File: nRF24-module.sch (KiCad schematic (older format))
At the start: 43 parts, among them SW1 SW_PUSH, U1 STM32F302C8T, U2 SN65HVD256, U3 NUF2042XV6, U4 MCP1700, U5 SiP32431, X1 16MHz 10ppm

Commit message: nRF pin assignment.
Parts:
- removed C10, C14, C16: 100nF, _std:_0603, symbol C
- removed C15: 1uF, _std:_0603, symbol C
- removed C6: 10nF, _std:_0603, symbol C
- removed CONN1: UART, _connectors:Molex-PicoBlade-4, symbol UART
- removed D3: V_BUS_PWR, _std:_0603, symbol LED
- removed R10, R11: 100, _std:_0603, symbol R
- removed R3, R4, R9: 10k, _std:_0603, symbol R
- removed R7: R, _std:_0603, symbol R
- removed U5: SiP32431, Housings_SOT-23_SOT-143_TSOT-6:SC-70-6, symbol SiP32431
- added D3, D4: BAT60J, _std:_SOD-323, symbol D
- added P1: CONN_02X04, Pin_Headers:Pin_Header_Straight_2x04, symbol CONN_02X04
- CONN2: renamed from CONN3; footprint _connectors:_Micro-USB-AB-receptacle-SMT-th -> _connectors:_Micro-USB-AB-receptacle-SMT
- D1: value STATUS -> nRF
- D2: value CAN1 -> CAN
- renumbered C13 to C10, C12 to C11, C5 to C4, C4 to C5, C7 to C6, C8 to C7, C9 to C8, C11 to C9, CONN2 to CONN1, CONN4 to CONN3, CONN5 to CONN4, R5 to R3, R6 to R4, R8 to R5
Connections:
- net labels added: +5V, CAN_ACTIVITY_LED, RF_ACTIVITY_LED, nRF_CE, nRF_CSN, nRF_IRQ, nRF_MISO, nRF_MOSI, nRF_SCK
- net labels removed: CAN1_PWR_LED, CAN1_STATUS_LED, CAN_SILENT, STATUS_LED, UART1_RX, UART1_TX, V_BUS_ENABLE, V_BUS_SENSE
- wire segments 109 -> 87
- no-connect marks 21 -> 23
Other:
- note added: "04.11.2015"
- note added: "<-JTCK"
- note added: "<-JTDI"
- note added: "<-JTDO"
- note added: "<-JTMS"
- note added: "<-JTRST"
- note added: "nRF24 module radio module"
- note removed: "(5V tolerant)"
- note removed: "25.10.2015"
- note removed: "CAN to USB adapter dongle"
- note removed: "Fc = 318 Hz\n(10k+10k)/(10k*10k*100nF*2*pi)"
- moved on the sheet: C10, C11, C9, CONN1, CONN2, CONN3, CONN4, F1, R5, U2, U3

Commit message: No dfu pushbutton
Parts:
- removed R2: 10k, _std:_0603, symbol R
- removed SW1: SW_PUSH, _div:PushButtonSMD-5x3mm, symbol SW_PUSH
- added C12: 22uF, _std:_0603, symbol C
- CONN1: footprint _connectors:_Solder_Pad1.27_5 -> _connectors:_Pin2mm_5z
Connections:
- net labels removed: BOOT0
- wire segments 87 -> 83
- no-connect marks 23 -> 24
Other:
- note removed: "enter dfu bootloader\nby pressing the button\nwhen plugging in the dongle"
- moved on the sheet: CONN1, D1, D2, D3, D4, P1, R3, R4

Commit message: Change voltage regulator
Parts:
- removed U4: MCP1700, _std:SOT-23, symbol MCP1700
- added U4: MCP1703, symbol MCP1703
- renumbered C9 to C10, C10 to C11, C11 to C12, C12 to C9, R3 to R2, R4 to R3, R5 to R4
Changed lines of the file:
@@
 $EndComp
 $Comp
-L R R4
+L R R3
 U 1 1 55622F4C
 P 5050 1650
-F 0 "R4" V 5130 1650 50  0000 C CNN
+F 0 "R3" V 5130 1650 50  0000 C CNN
 F 1 "R" V 5050 1650 50  0000 C CNN
 F 2 "_std:_0603" V 4980 1650 30  0001 C CNN
@@
 $EndComp
 $Comp
-L R R3
+L R R2
 U 1 1 5562427A
 P 5050 1350
-F 0 "R3" V 5130 1350 50  0000 C CNN
+F 0 "R2" V 5130 1350 50  0000 C CNN
 F 1 "R" V 5050 1350 50  0000 C CNN
 F 2 "_std:_0603" V 4980 1350 30  0001 C CNN
@@
 $EndComp
 $Comp
-L MCP1700 U4
-U 1 1 55D2FCCD
-P 9400 1600
-F 0 "U4" H 9650 1800 60  0000 C CNN
-F 1 "MCP1700" H 9350 1800 60  0000 C CNN
-F 2 "_std:SOT-23" H 9300 2050 60  0001 C CNN
-F 3 "" H 9300 2050 60  0000 C CNN
-	1    9400 1600
-	1    0    0    -1
-$EndComp
-$Comp
-L C C9
+L C C10
 U 1 1 55D2FDCA
 P 8850 1750
-F 0 "C9" H 8875 1850 50  0000 L CNN
+F 0 "C10" H 8875 1850 50  0000 L CNN
 F 1 "1uF" H 8875 1650 50  0000 L CNN
 F 2 "_std:_0603" H 8888 1600 30  0001 C CNN
@@
 $EndComp
 $Comp
-L C C11
+L C C12
 U 1 1 55D2FE2A
 P 9950 1750
-F 0 "C11" H 9975 1850 50  0000 L CNN
+F 0 "C12" H 9975 1850 50  0000 L CNN
 F 1 "1uF" H 9975 1650 50  0000 L CNN
 F 2 "_std:_0603" H 9988 1600 30  0001 C CNN
@@
 Author: Michael Spieler
 $Comp
-L C C10
+L C C11
 U 1 1 560BF88C
 P 9750 2950
-F 0 "C10" H 9800 2850 50  0000 L CNN
+F 0 "C11" H 9800 2850 50  0000 L CNN
 F 1 "100nF" V 9600 2850 50  0000 L CNN
 F 2 "_std:_0603" H 9788 2800 30  0001 C CNN
@@
 $EndComp
 $Comp
-L R R5
+L R R4
 U 1 1 560C3883
 P 8000 3000
-F 0 "R5" V 8080 3000 50  0000 C CNN
+F 0 "R4" V 8080 3000 50  0000 C CNN
 F 1 "1.5k" V 8000 3000 50  0000 C CNN
 F 2 "_std:_0603" V 7930 3000 30  0001 C CNN
@@
 NoConn ~ 3600 4900
 NoConn ~ 3600 3500
-$Comp
-L CVRA_logo #G1
-U 1 1 562D3733
-P 10100 6850
-F 0 "#G1" H 10100 6682 60  0001 C CNN
-F 1 "CVRA_logo" H 10100 7018 60  0001 C CNN
-F 2 "" H 10100 6850 60  0000 C CNN
-F 3 "" H 10100 6850 60  0000 C CNN
-	1    10100 6850
-	1    0    0    -1
-$EndComp
 $Comp
 L STM32F302C8T U1
@@
 Wire Wire Line
 	9950 1950 9950 1900
-Connection ~ 9400 1950
 Wire Wire Line
 	9850 5650 9950 5650
@@
 Connection ~ 7750 4650
 $Comp
-L C C12
+L C C9
 U 1 1 563B4E3B
 P 8600 1750
-F 0 "C12" H 8625 1850 50  0000 L CNN
+F 0 "C9" H 8625 1850 50  0000 L CNN
 F 1 "22uF" H 8625 1650 50  0000 L CNN
 F 2 "_std:_0603" H 8638 1600 30  0001 C CNN
@@
 $EndComp
 NoConn ~ 3600 1400
+$Comp
+L MCP1703 U4
+U 1 1 563B6919
+P 9400 1600
+F 0 "U4" H 9650 1800 60  0000 C CNN
+F 1 "MCP1703" H 9350 1800 60  0000 C CNN
+F 2 "" H 9300 2050 60  0000 C CNN
+F 3 "" H 9300 2050 60  0000 C CNN
+	1    9400 1600
+	1    0    0    -1
+$EndComp
+Connection ~ 9400 1950
 $EndSCHEMATC

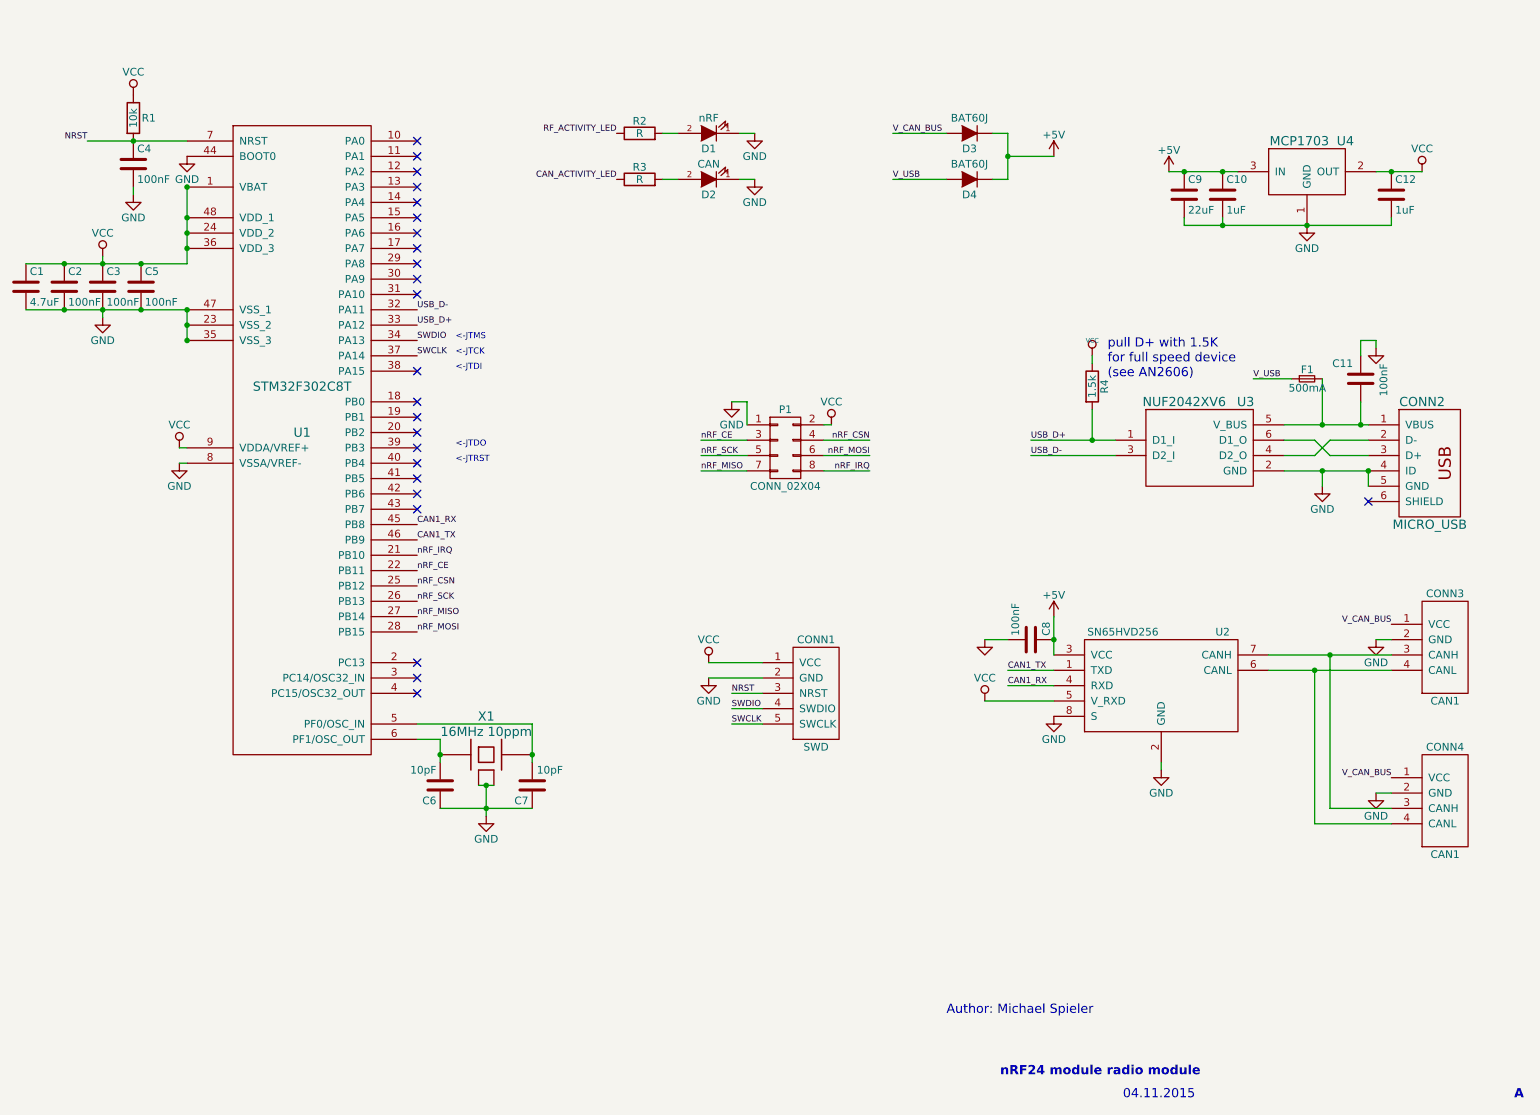
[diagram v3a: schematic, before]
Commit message: Simplify schematic
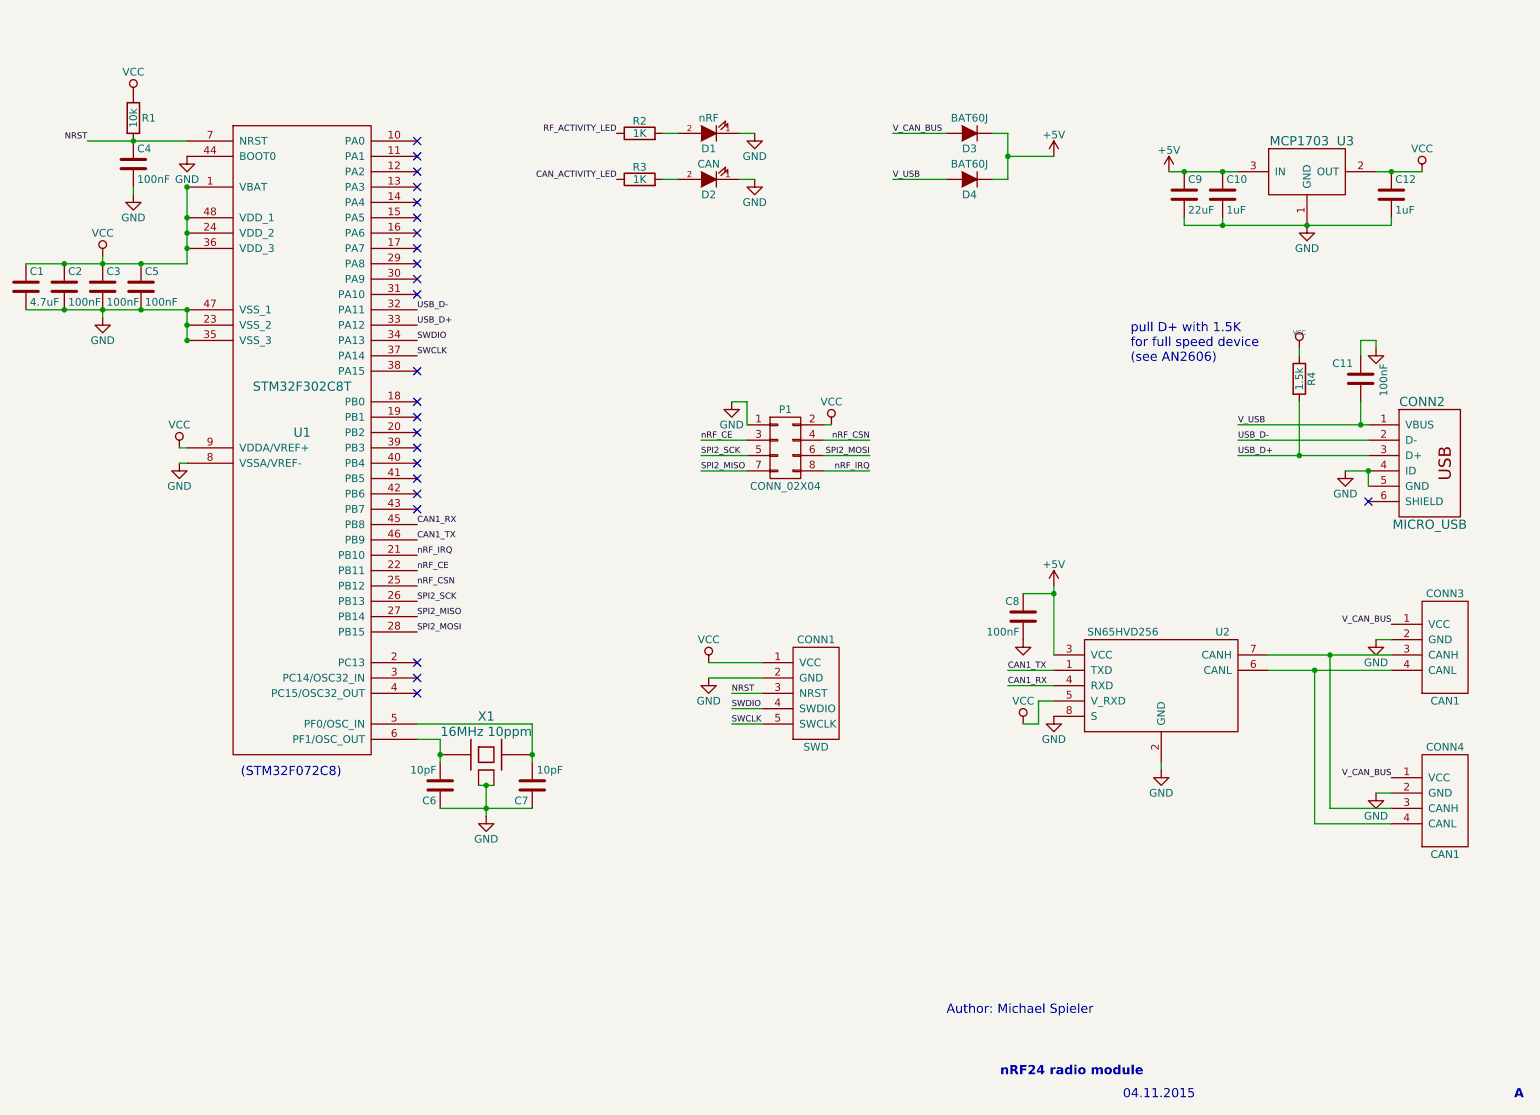
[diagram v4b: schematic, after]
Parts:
- removed F1: 500mA, Resistors_SMD:R_0805, symbol F_Small
- removed U3: NUF2042XV6, _std:SOT-563_6-lead, symbol NUF2042XV6
- R2, R3: value R -> 1K
- renumbered U4 to U3
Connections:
- net USB_D+: now also CONN2.3 (D+)
- net USB_D-: now also CONN2.2 (D-)
- net V_USB: now also C11.1, CONN2.1 (VBUS)
- net nRF_MISO renamed SPI2_MISO
- net nRF_MOSI renamed SPI2_MOSI
- net nRF_SCK renamed SPI2_SCK
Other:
- note added: "(STM32F072C8)"
- note added: "nRF24 radio module"
- note removed: "<-JTCK"
- note removed: "<-JTDI"
- note removed: "<-JTDO"
- note removed: "<-JTMS"
- note removed: "<-JTRST"
- note removed: "nRF24 module radio module"
- moved on the sheet: C8, R4
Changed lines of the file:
@@
 Text Label 3600 2600 0    40   ~ 0
 USB_D+
-Text Label 7600 3450 0    40   ~ 0
+Text Label 8950 3350 0    40   ~ 0
 USB_D-
-Text Label 7600 3350 0    40   ~ 0
+Text Label 8950 3450 0    40   ~ 0
 USB_D+
-Text Label 9050 2950 0    40   ~ 0
+Text Label 8950 3250 0    40   ~ 0
 V_USB
 $Comp
 L GND #PWR08
 U 1 1 55621D6C
-P 9500 3650
-F 0 "#PWR08" H 9500 3400 50  0001 C CNN
-F 1 "GND" H 9500 3500 50  0000 C CNN
-F 2 "" H 9500 3650 60  0000 C CNN
-F 3 "" H 9500 3650 60  0000 C CNN
-	1    9500 3650
+P 9650 3550
+F 0 "#PWR08" H 9650 3300 50  0001 C CNN
+F 1 "GND" H 9650 3400 50  0000 C CNN
+F 2 "" H 9650 3550 60  0000 C CNN
+F 3 "" H 9650 3550 60  0000 C CNN
+	1    9650 3550
 	1    0    0    -1
 $EndComp
@@
 P 5050 1650
 F 0 "R3" V 5130 1650 50  0000 C CNN
-F 1 "R" V 5050 1650 50  0000 C CNN
+F 1 "1K" V 5050 1650 50  0000 C CNN
 F 2 "_std:_0603" V 4980 1650 30  0001 C CNN
 F 3 "" H 5050 1650 30  0000 C CNN
@@
 P 5050 1350
 F 0 "R2" V 5130 1350 50  0000 C CNN
-F 1 "R" V 5050 1350 50  0000 C CNN
+F 1 "1K" V 5050 1350 50  0000 C CNN
 F 2 "_std:_0603" V 4980 1350 30  0001 C CNN
 F 3 "" H 5050 1350 30  0000 C CNN
@@
 L VCC #PWR011
 U 1 1 5592BB1F
-P 7300 5050
-F 0 "#PWR011" H 7300 4900 50  0001 C CNN
-F 1 "VCC" H 7300 5200 50  0000 C CNN
-F 2 "" H 7300 5050 60  0000 C CNN
-F 3 "" H 7300 5050 60  0000 C CNN
-	1    7300 5050
+P 7550 5200
+F 0 "#PWR011" H 7550 5050 50  0001 C CNN
+F 1 "VCC" H 7550 5350 50  0000 C CNN
+F 2 "" H 7550 5200 60  0000 C CNN
+F 3 "" H 7550 5200 60  0000 C CNN
+	1    7550 5200
 	1    0    0    -1
 $EndComp
@@
 Text Label 6700 1650 0    40   ~ 0
 V_USB
-$Comp
-L F_Small F1
-U 1 1 55D30CFC
-P 9400 2950
-F 0 "F1" H 9360 3010 50  0000 L CNN
-F 1 "500mA" H 9280 2890 50  0000 L CNN
-F 2 "Resistors_SMD:R_0805" H 9400 2950 60  0001 C CNN
-F 3 "" H 9400 2950 60  0000 C CNN
-	1    9400 2950
-	1    0    0    -1
-$EndComp
 Text Label 6700 1350 0    40   ~ 0
 V_CAN_BUS
@@
 $EndComp
 Text Notes 7400 7500 0    60   ~ 12
-nRF24 module radio module
+nRF24 radio module
 Text Notes 10750 7650 0    60   ~ 12
 A
@@
 L R R4
 U 1 1 560C3883
-P 8000 3000
-F 0 "R4" V 8080 3000 50  0000 C CNN
-F 1 "1.5k" V 8000 3000 50  0000 C CNN
-F 2 "_std:_0603" V 7930 3000 30  0001 C CNN
-F 3 "" H 8000 3000 30  0000 C CNN
-	1    8000 3000
+P 9350 2950
+F 0 "R4" V 9430 2950 50  0000 C CNN
+F 1 "1.5k" V 9350 2950 50  0000 C CNN
+F 2 "_std:_0603" V 9280 2950 30  0001 C CNN
+F 3 "" H 9350 2950 30  0000 C CNN
+	1    9350 2950
 	1    0    0    -1
 $EndComp
@@
 L VCC #PWR017
 U 1 1 560C391D
-P 8000 2800
-F 0 "#PWR017" H 8000 2900 30  0001 C CNN
-F 1 "VCC" H 8000 2900 30  0000 C CNN
-F 2 "" H 8000 2800 60  0000 C CNN
-F 3 "" H 8000 2800 60  0000 C CNN
-	1    8000 2800
-	1    0    0    -1
-$EndComp
-Text Notes 8100 2950 0    60   ~ 0
+P 9350 2750
+F 0 "#PWR017" H 9350 2850 30  0001 C CNN
+F 1 "VCC" H 9350 2850 30  0000 C CNN
+F 2 "" H 9350 2750 60  0000 C CNN
+F 3 "" H 9350 2750 60  0000 C CNN
+	1    9350 2750
+	1    0    0    -1
+$EndComp
+Text Notes 8250 2850 0    60   ~ 0
 pull D+ with 1.5K\nfor full speed device\n(see AN2606)
 NoConn ~ 3600 5000
@@
 NoConn ~ 9800 3750
 $Comp
-L NUF2042XV6 U3
-U 1 1 560EE9C9
-P 8700 3400
-F 0 "U3" H 9000 3700 60  0000 C CNN
-F 1 "NUF2042XV6" H 8600 3700 60  0000 C CNN
-F 2 "_std:SOT-563_6-lead" H 8700 3300 60  0001 C CNN
-F 3 "" H 8700 3300 60  0000 C CNN
-	1    8700 3400
-	1    0    0    -1
-$EndComp
-$Comp
 L C C8
 U 1 1 560F039C
-P 7600 4650
-F 0 "C8" H 7625 4750 50  0000 L CNN
-F 1 "100nF" H 7625 4550 50  0000 L CNN
-F 2 "_std:_0603" H 7638 4500 30  0001 C CNN
-F 3 "" H 7600 4650 60  0000 C CNN
-	1    7600 4650
-	0    1    -1   0
+P 7550 4500
+F 0 "C8" H 7575 4600 50  0000 L CNN
+F 1 "100nF" H 7575 4400 50  0000 L CNN
+F 2 "_std:_0603" H 7588 4350 30  0001 C CNN
+F 3 "" H 7550 4500 60  0000 C CNN
+	1    7550 4500
+	-1   0    0    -1
 $EndComp
 $Comp
 L GND #PWR018
 U 1 1 560F050D
-P 7300 4650
-F 0 "#PWR018" H 7300 4650 30  0001 C CNN
-F 1 "GND" H 7300 4580 30  0001 C CNN
-F 2 "" H 7300 4650 60  0000 C CNN
-F 3 "" H 7300 4650 60  0000 C CNN
-	1    7300 4650
+P 7550 4650
+F 0 "#PWR018" H 7550 4650 30  0001 C CNN
+F 1 "GND" H 7550 4580 30  0001 C CNN
+F 2 "" H 7550 4650 60  0000 C CNN
+F 3 "" H 7550 4650 60  0000 C CNN
+	1    7550 4650
 	1    0    0    -1
 $EndComp
@@
 	1    0    0    -1
 $EndComp
-NoConn ~ 3600 3700
-NoConn ~ 3600 3800
 NoConn ~ 3600 3400
 NoConn ~ 3600 3600
@@
 Text Label 6550 3550 2    40   ~ 0
 nRF_IRQ
-Text Label 6550 3450 2    40   ~ 0
-nRF_MOSI
-Text Label 5450 3550 0    40   ~ 0
-nRF_MISO
-Text Label 5450 3450 0    40   ~ 0
-nRF_SCK
 Text Label 6550 3350 2    40   ~ 0
 nRF_CSN
@@
 nRF_CE
 Text Label 3600 4400 0    40   ~ 0
-nRF_SCK
+SPI2_SCK
 Text Label 3600 4500 0    40   ~ 0
-nRF_MISO
+SPI2_MISO
 Text Label 3600 4300 0    40   ~ 0
 nRF_CSN
 Text Label 3600 4600 0    40   ~ 0
-nRF_MOSI
+SPI2_MOSI
 Text Label 3600 4100 0    40   ~ 0
 nRF_IRQ
@@
 NoConn ~ 3600 1600
 NoConn ~ 3600 2900
-Text Notes 3850 2700 0    40   ~ 0
-<-JTMS
-Text Notes 3850 2800 0    40   ~ 0
-<-JTCK
-Text Notes 3850 2900 0    40   ~ 0
-<-JTDI
-Text Notes 3850 3500 0    40   ~ 0
-<-JTRST
-Text Notes 3850 3400 0    40   ~ 0
-<-JTDO
 $Comp
 L +5V #PWR025
@@
 	1    0    0    -1
 $EndComp
+$Comp
+L +5V #PWR027
+U 1 1 563B3A0E
+P 7750 4300
+F 0 "#PWR027" H 7750 4150 50  0001 C CNN
+F 1 "+5V" H 7750 4440 50  0000 C CNN
+F 2 "" H 7750 4300 60  0000 C CNN
+F 3 "" H 7750 4300 60  0000 C CNN
+	1    7750 4300
+	1    0    0    -1
+$EndComp
+$Comp
+L C C9
+U 1 1 563B4E3B
+P 8600 1750
+F 0 "C9" H 8625 1850 50  0000 L CNN
+F 1 "22uF" H 8625 1650 50  0000 L CNN
+F 2 "_std:_0603" H 8638 1600 30  0001 C CNN
+F 3 "" H 8600 1750 60  0000 C CNN
+	1    8600 1750
+	1    0    0    -1
+$EndComp
+$Comp
+L GND #PWR028
+U 1 1 563B55C7
+P 2100 1500
+F 0 "#PWR028" H 2100 1250 50  0001 C CNN
+F 1 "GND" H 2100 1350 50  0000 C CNN
+F 2 "" H 2100 1500 60  0000 C CNN
+F 3 "" H 2100 1500 60  0000 C CNN
+	1    2100 1500
+	1    0    0    -1
+$EndComp
+NoConn ~ 3600 1400
+$Comp
+L MCP1703 U3
+U 1 1 563B6919
+P 9400 1600
+F 0 "U3" H 9650 1800 60  0000 C CNN
+F 1 "MCP1703" H 9350 1800 60  0000 C CNN
+F 2 "" H 9300 2050 60  0000 C CNN
+F 3 "" H 9300 2050 60  0000 C CNN
+	1    9400 1600
+	1    0    0    -1
+$EndComp
+Text Notes 2450 5550 0    60   ~ 0
+(STM32F072C8)
+NoConn ~ 3600 3800
+NoConn ~ 3600 3700
 Wire Wire Line
 	5500 4900 5850 4900
@@
 	8450 5450 8450 5500
 Wire Wire Line
-	7300 5050 7750 5050
-Wire Wire Line
 	9850 4650 9950 4650
 Connection ~ 8850 1600
@@
 Connection ~ 9450 4850
 Wire Wire Line
-	7600 3450 8150 3450
-Wire Wire Line
-	7600 3350 8150 3350
+	8950 3350 9800 3350
+Wire Wire Line
+	8950 3450 9800 3450
 Connection ~ 9750 3250
 Wire Wire Line
@@
 	9850 2700 9850 2750
 Wire Wire Line
-	8000 2800 8000 2850
-Wire Wire Line
-	9500 3650 9500 3550
+	9350 2750 9350 2800
 Wire Wire Line
 	9800 3550 9800 3650
 Wire Wire Line
-	9250 3250 9800 3250
-Wire Wire Line
-	9250 3550 9800 3550
+	8950 3250 9800 3250
 Connection ~ 9800 3550
 Wire Wire Line
-	9500 2950 9500 3250
-Connection ~ 9500 3250
-Connection ~ 9500 3550
-Wire Wire Line
 	7450 4850 7750 4850
 Wire Wire Line
 	7750 4950 7450 4950
-Wire Wire Line
-	9050 2950 9300 2950
 Wire Wire Line
 	4000 5600 4100 5600
@@
 	1550 2150 1550 2200
 Wire Wire Line
-	8000 3150 8000 3350
-Connection ~ 8000 3350
-Wire Wire Line
-	9250 3350 9450 3350
-Wire Wire Line
-	9450 3350 9550 3450
-Wire Wire Line
-	9550 3450 9800 3450
-Wire Wire Line
-	9800 3350 9550 3350
-Wire Wire Line
-	9550 3350 9450 3450
-Wire Wire Line
-	9450 3450 9250 3450
+	9350 3100 9350 3450
+Connection ~ 9350 3450
 Wire Wire Line
 	5200 1650 5300 1650
 Wire Wire Line
 	5200 1350 5300 1350
-Wire Wire Line
-	7300 4650 7450 4650
-Wire Wire Line
-	7750 4500 7750 4750
 Wire Wire Line
 	2050 3400 2100 3400
@@
 Wire Wire Line
 	8500 1600 8950 1600
-$Comp
-L +5V #PWR027
-U 1 1 563B3A0E
-P 7750 4500
-F 0 "#PWR027" H 7750 4350 50  0001 C CNN
-F 1 "+5V" H 7750 4640 50  0000 C CNN
-F 2 "" H 7750 4500 60  0000 C CNN
-F 3 "" H 7750 4500 60  0000 C CNN
-	1    7750 4500
-	1    0    0    -1
-$EndComp
-Connection ~ 7750 4650
-$Comp
-L C C9
-U 1 1 563B4E3B
-P 8600 1750
-F 0 "C9" H 8625 1850 50  0000 L CNN
-F 1 "22uF" H 8625 1650 50  0000 L CNN
-F 2 "_std:_0603" H 8638 1600 30  0001 C CNN
-F 3 "" H 8600 1750 60  0000 C CNN
-	1    8600 1750
-	1    0    0    -1
-$EndComp
 Connection ~ 8600 1600
 Wire Wire Line
 	8600 1900 8600 1950
 Connection ~ 8850 1950
-$Comp
-L GND #PWR028
-U 1 1 563B55C7
-P 2100 1500
-F 0 "#PWR028" H 2100 1250 50  0001 C CNN
-F 1 "GND" H 2100 1350 50  0000 C CNN
-F 2 "" H 2100 1500 60  0000 C CNN
-F 3 "" H 2100 1500 60  0000 C CNN
-	1    2100 1500
-	1    0    0    -1
-$EndComp
-NoConn ~ 3600 1400
-$Comp
-L MCP1703 U4
-U 1 1 563B6919
-P 9400 1600
-F 0 "U4" H 9650 1800 60  0000 C CNN
-F 1 "MCP1703" H 9350 1800 60  0000 C CNN
-F 2 "" H 9300 2050 60  0000 C CNN
-F 3 "" H 9300 2050 60  0000 C CNN
-	1    9400 1600
-	1    0    0    -1
-$EndComp
 Connection ~ 9400 1950
+Wire Wire Line
+	9800 3550 9650 3550
+Wire Wire Line
+	7750 5050 7650 5050
+Wire Wire Line
+	7650 5050 7650 5200
+Wire Wire Line
+	7650 5200 7550 5200
+Wire Wire Line
+	7550 4350 7750 4350
+Connection ~ 7750 4350
+Wire Wire Line
+	7750 4300 7750 4750
+Text Label 5450 3550 0    40   ~ 0
+SPI2_MISO
+Text Label 6550 3450 2    40   ~ 0
+SPI2_MOSI
+Text Label 5450 3450 0    40   ~ 0
+SPI2_SCK
 $EndSCHEMATC
